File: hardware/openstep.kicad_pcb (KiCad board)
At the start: 2 copper layers, 60 x 60 mm, 74 parts, among them J1 DB-15M, J2 Chain IN, J3 Chain OUT, J4 AVRISP, U1 LM1117-5.0, U2 MCP6004, U3 MCP6004, U4 MCP6002, U5 MCP3208, U7 ATmega32U4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

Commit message: second board revision, fixed power supply stuff
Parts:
- added C18: 100p, smd_capacitors:c_0603, F.Cu at (115.1, 118.6)
- added CON1: BARREL_JACK, footprints:LUMBERG_1613_14, F.Cu at (109.2, 127.7)
- added L1: INDUCTOR_SMALL, libcms:SM1206, F.Cu at (108.7, 115.6)
- added L2: INDUCTOR_SMALL, libcms:SM1206, F.Cu at (119.4, 125.3)
- S1: value Reset -> SW6x6
- moved U1 18.7 mm to (122.2, 117.6), turned to 270 degrees
- moved C9 11.3 mm to (116.8, 110.5), turned to 270 degrees
- moved C1 9.72 mm to (112.8, 114.6), turned to 270 degrees
- moved C14 2.07 mm to (97.0, 114.0)
- moved R21 2.03 mm to (105.9, 72.6)
- moved AVCC 2.03 mm to (102.4, 72.6)
- moved DVCC 2.03 mm to (107.7, 72.6)
- moved R22 2.03 mm to (104.1, 72.6)
- moved R18 1.66 mm to (100.1, 112.5)
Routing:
- net GND: track 112.7 -> 78.4 mm, vias 16 -> 15
- net +5VA: track 125.0 -> 156.1 mm
- net Net-(C18-Pad1): track 0.00 -> 22.5 mm
- net VSS: track 195.0 -> 215.4 mm
- net Net-(C18-Pad2): track 0.00 -> 14.3 mm
- net /V_IN: track 3.71 -> 11.4 mm
- net (no net): track 3.25 -> 0.00 mm, vias 2 -> 0
- net Net-(C14-Pad2): track 15.6 -> 18.4 mm
- net GNDA: track 198.0 -> 196.5 mm
- net /MISO: track 102.4 -> 101.0 mm
- net Net-(C14-Pad1): track 23.1 -> 22.1 mm
- net /MOSI: track 108.4 -> 107.6 mm

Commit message: foo
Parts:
- added G***: LOGO, footprints:frob, F.Cu at (115.4, 87.2)
- added G***: LOGO, footprints:nsa_inside, F.Cu at (92.8, 99.3)
- added G***: LOGO, footprints:electricity-girl, B.Cu at (100.1, 100.1)
- added G***: LOGO, footprints:electricity-arrow, B.Cu at (100.1, 100.1)
- renumbered CON1 to J5
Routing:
- net +5VA: track 156.1 -> 157.0 mm
- net /SCK: track 100.7 -> 100.0 mm
- net /MISO: track 101.0 -> 100.4 mm
- net /MOSI: track 107.6 -> 107.0 mm
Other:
- board text added: "2016 github.com/jaseg cc-by-sa"
- board text added: "ISP"
- board text added: "v2.0 CCCB cyber-spezial edition"
- board text removed: "2016 jaseg"
- board text removed: "CC-BY-SA"
- board text removed: "v2.0"

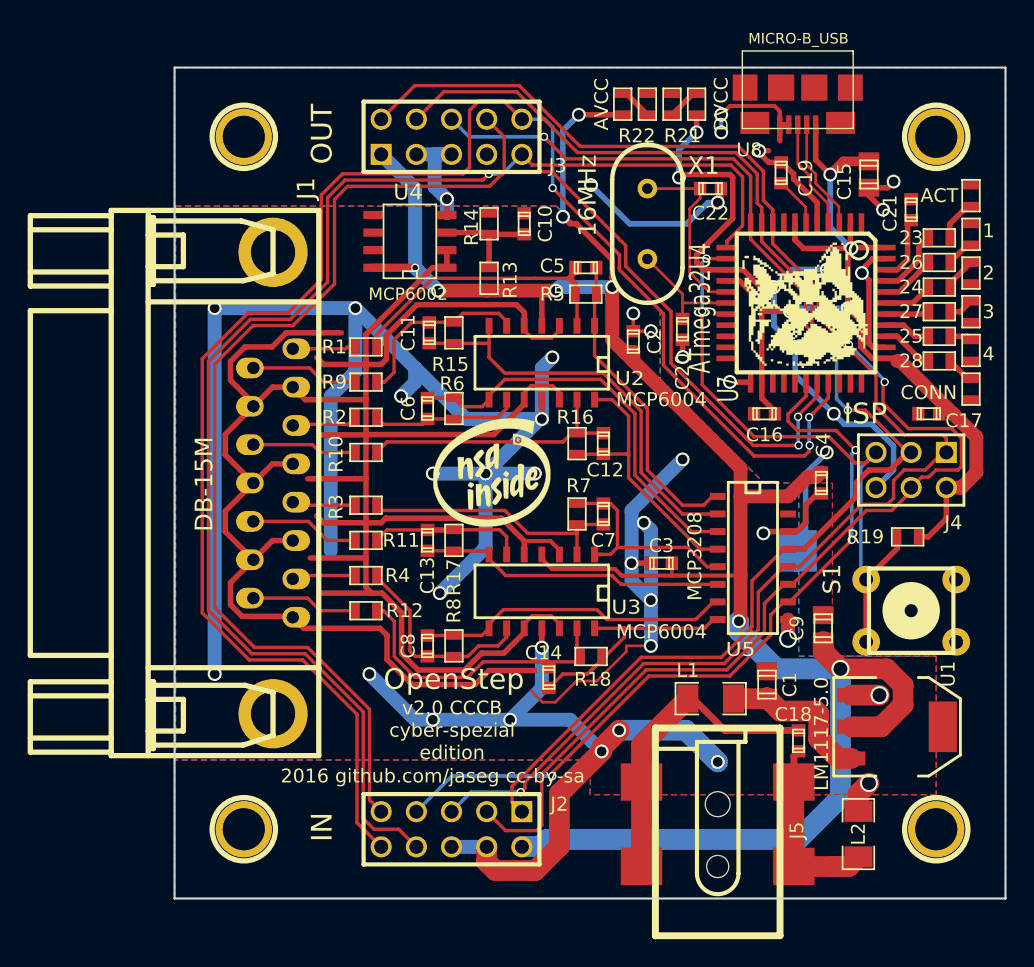
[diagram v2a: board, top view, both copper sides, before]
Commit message: fixed chain conn orientation
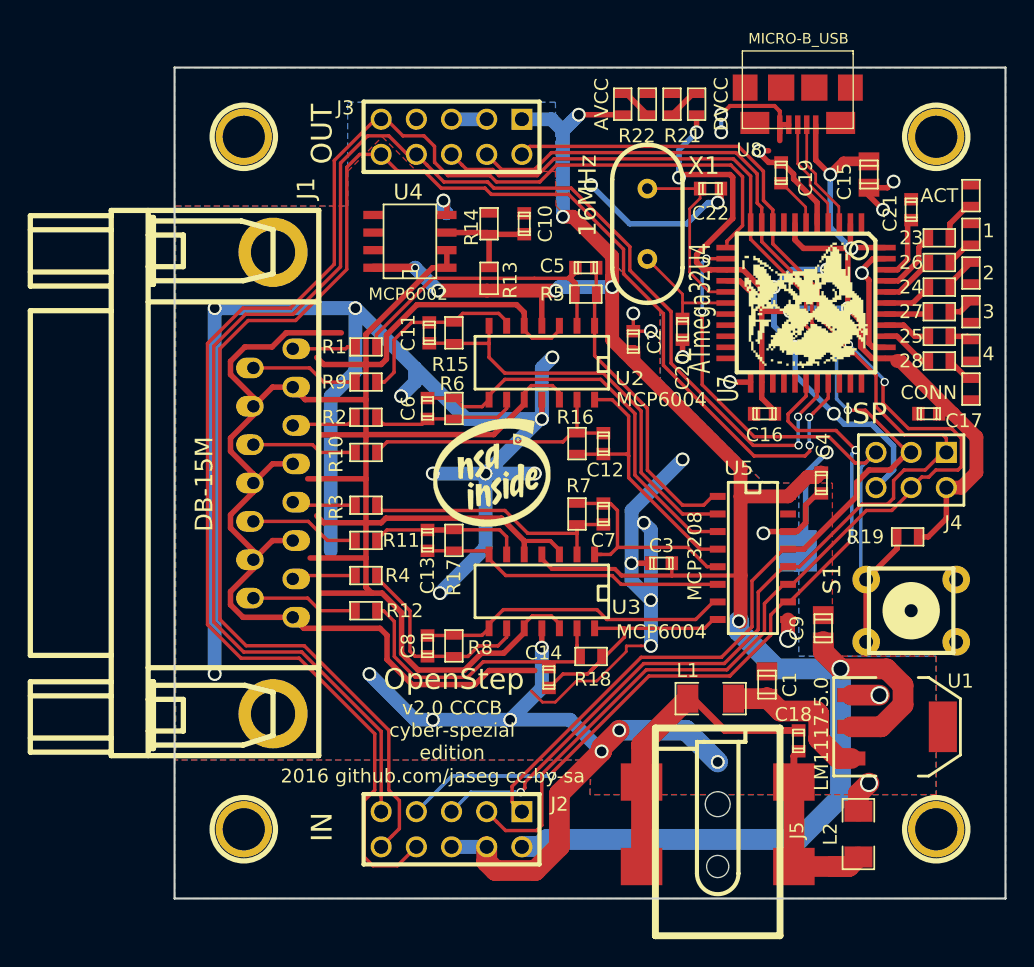
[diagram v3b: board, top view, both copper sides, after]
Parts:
- turned J3 to 180 degrees
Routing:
- net /SCK: track 100.0 -> 87.3 mm
- net /ADC_CS3: track 99.2 -> 108.2 mm, vias 1 -> 0
- net /ADC_CS2: track 122.1 -> 115.0 mm, vias 3 -> 2
- net /MOSI: track 107.0 -> 100.3 mm
- net +5VA: track 157.0 -> 151.2 mm
- net VSS: track 215.4 -> 210.6 mm
- net GNDA: track 196.5 -> 195.9 mm
- net /MISO: vias 2 -> 1

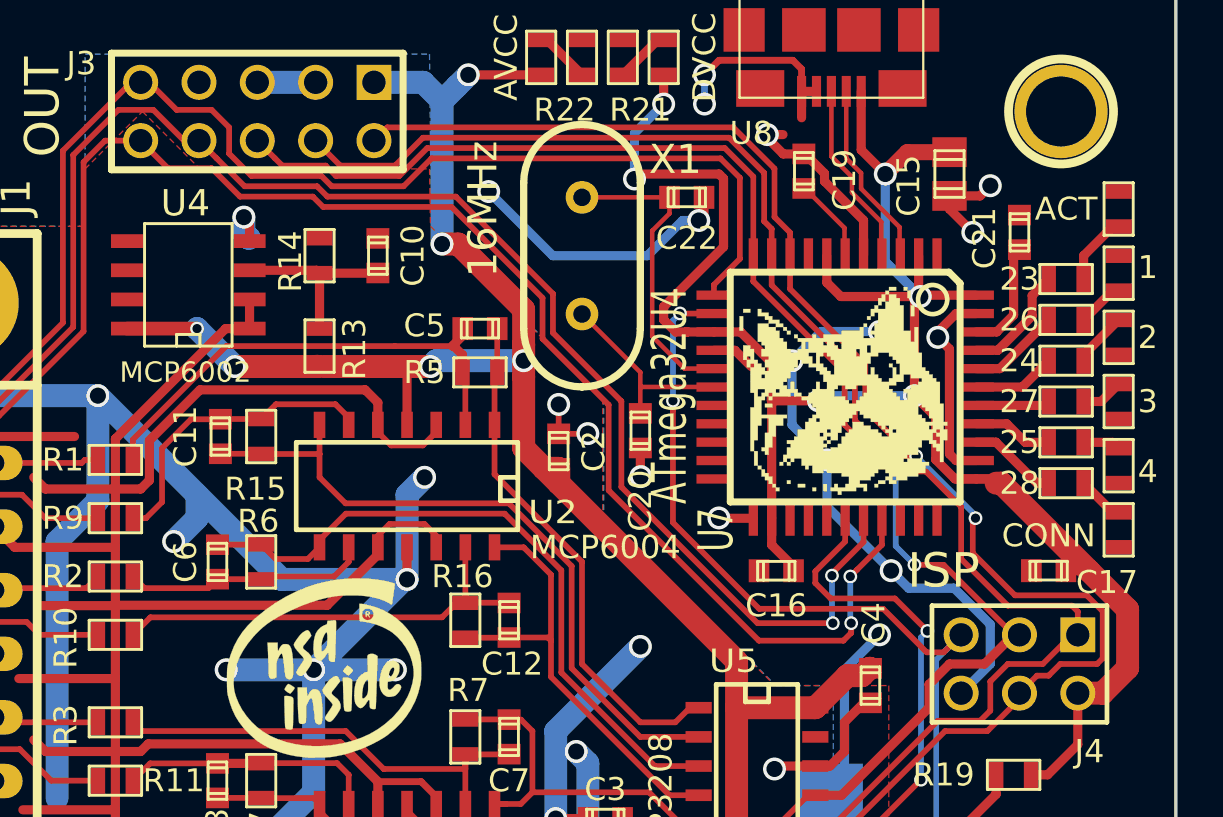
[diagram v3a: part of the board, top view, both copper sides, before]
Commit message: Add some more testpads for the CPU
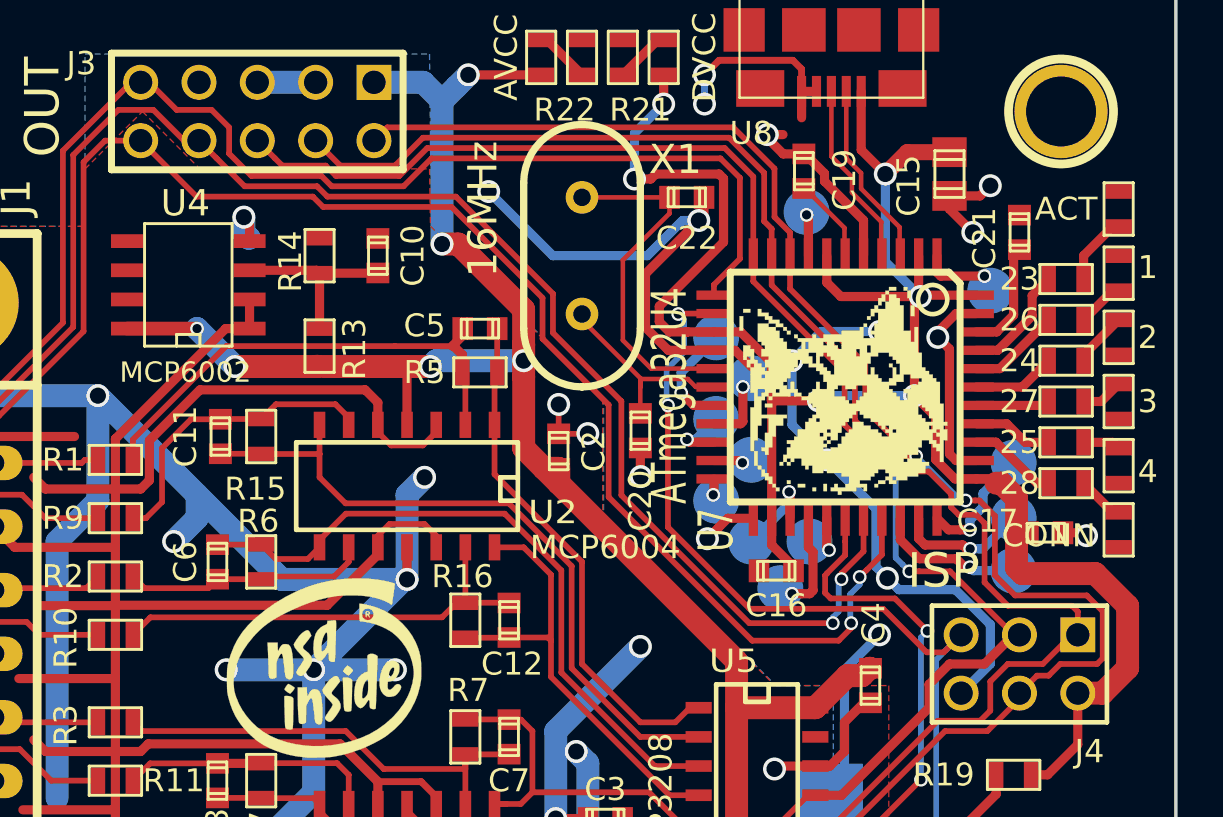
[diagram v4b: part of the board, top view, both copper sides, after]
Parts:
- added P1: CONN_1, footprints:TP_OPENSTEP, B.Cu at (122.9, 95.0)
- added P10: CONN_1, footprints:TP_OPENSTEP, B.Cu at (114.0, 93.7)
- added P11: CONN_1, footprints:TP_OPENSTEP, B.Cu at (122.9, 90.3)
- added P12: CONN_1, footprints:TP_OPENSTEP, B.Cu at (121.9, 82.8)
- added P13: CONN_1, footprints:TP_OPENSTEP, B.Cu at (113.9, 79.4)
- added P2: CONN_1, footprints:TP_OPENSTEP, B.Cu at (122.9, 92.7)
- added P3: CONN_1, footprints:TP_OPENSTEP, B.Cu at (110.0, 84.8)
- added P4: CONN_1, footprints:TP_OPENSTEP, B.Cu at (111.5, 86.6)
- added P5: CONN_1, footprints:TP_OPENSTEP, B.Cu at (110.0, 88.4)
- added P6: CONN_1, footprints:TP_OPENSTEP, B.Cu at (111.5, 90.2)
- added P7: CONN_1, footprints:TP_OPENSTEP, B.Cu at (111.5, 93.7)
- added P8: CONN_1, footprints:TP_OPENSTEP, B.Cu at (110.0, 91.9)
- added P9: CONN_1, footprints:TP_OPENSTEP, B.Cu at (112.8, 95.8)
- moved C17 1.66 mm to (124.3, 93.3), turned to 180 degrees
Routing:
- net GND: track 78.4 -> 89.6 mm, vias 15 -> 16
- net Net-(P1-Pad1): track 0.00 -> 6.43 mm, vias 0 -> 1
- net Net-(P2-Pad1): track 0.00 -> 5.76 mm, vias 0 -> 1
- net Net-(P11-Pad1): track 0.00 -> 5.35 mm, vias 0 -> 1
- net Net-(P3-Pad1): track 0.00 -> 4.70 mm, vias 0 -> 1
- net Net-(P9-Pad1): track 0.00 -> 4.20 mm, vias 0 -> 1
- net Net-(P7-Pad1): track 0.00 -> 4.01 mm, vias 0 -> 1
- net Net-(P5-Pad1): track 0.00 -> 2.86 mm, vias 0 -> 1
- net Net-(P12-Pad1): track 0.00 -> 2.86 mm, vias 0 -> 1
- net Net-(P4-Pad1): track 0.00 -> 2.81 mm, vias 0 -> 1
- net +5VD: track 89.9 -> 91.9 mm
- net Net-(C22-Pad1): track 13.5 -> 15.4 mm
- net Net-(P13-Pad1): track 0.00 -> 1.82 mm, vias 0 -> 1
- net Net-(P10-Pad1): track 0.00 -> 1.42 mm, vias 0 -> 1
- net Net-(P6-Pad1): track 0.00 -> 1.28 mm, vias 0 -> 1
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
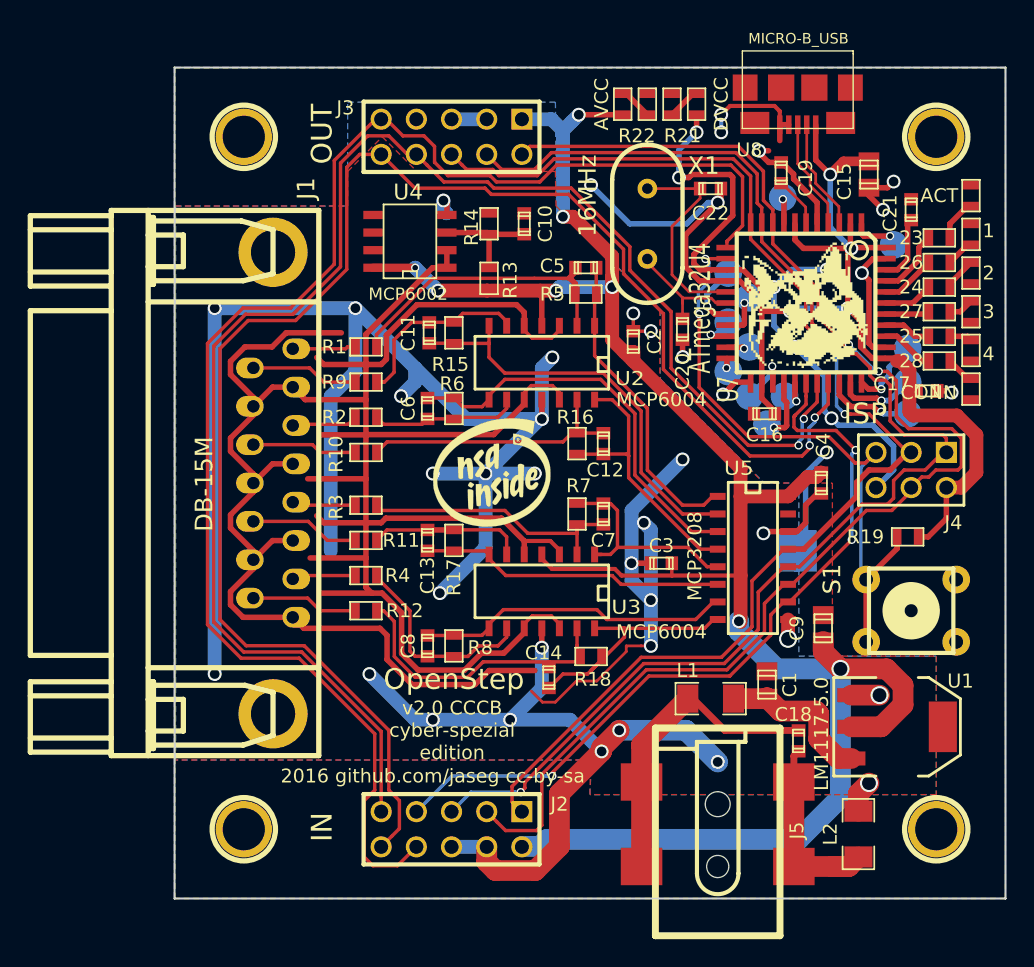
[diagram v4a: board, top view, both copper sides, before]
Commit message: Prettified AVCC routing a bit
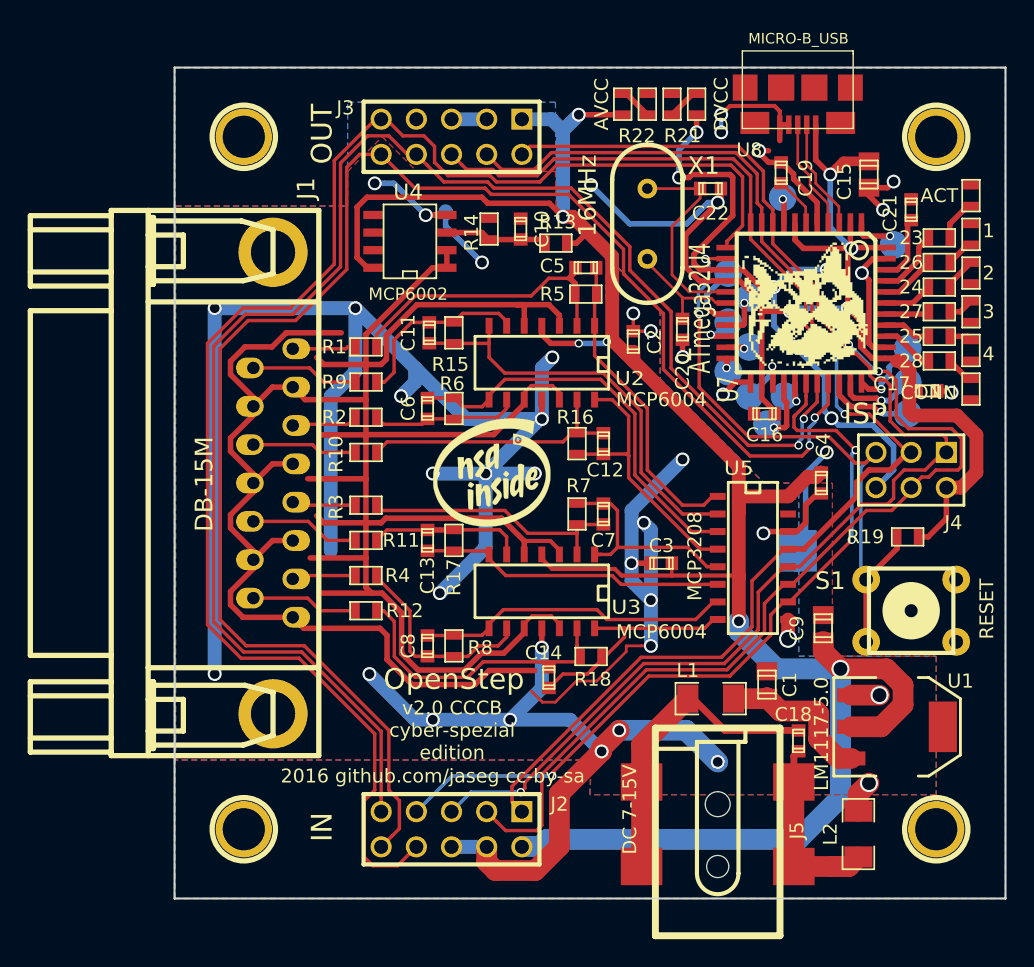
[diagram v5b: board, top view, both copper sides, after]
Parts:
- moved R13 5.45 mm to (97.5, 82.7), turned to 180 degrees
- moved C10 0.46 mm to (95.0, 81.7)
- moved R14 0.38 mm to (92.7, 81.7)
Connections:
- U4 pad 5: (no net) -> VSS
- U4 pad 6: (no net) -> VSS
- U4 pad 7: (no net) -> Net-(U4-Pad7)
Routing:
- net VSS: track 210.6 -> 221.1 mm, vias 29 -> 31
- net +5VA: track 151.0 -> 161.3 mm, vias 8 -> 6
- net GNDA: track 195.9 -> 197.3 mm
- net Net-(C10-Pad1): track 8.06 -> 7.44 mm
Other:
- board text added: "DC 7-15V"
- board text added: "RESET"

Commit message: Minor layout tweaks
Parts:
- moved C4 0.20 mm to (116.7, 100.2)
